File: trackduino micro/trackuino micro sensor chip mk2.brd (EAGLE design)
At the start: 49.8 x 19 mm, 41 parts, among them IC2 74AHC1G125DBV, SW1 SPST_TACT-KMR2, U1 ATMEGA168MLF, Y1 16MHZ

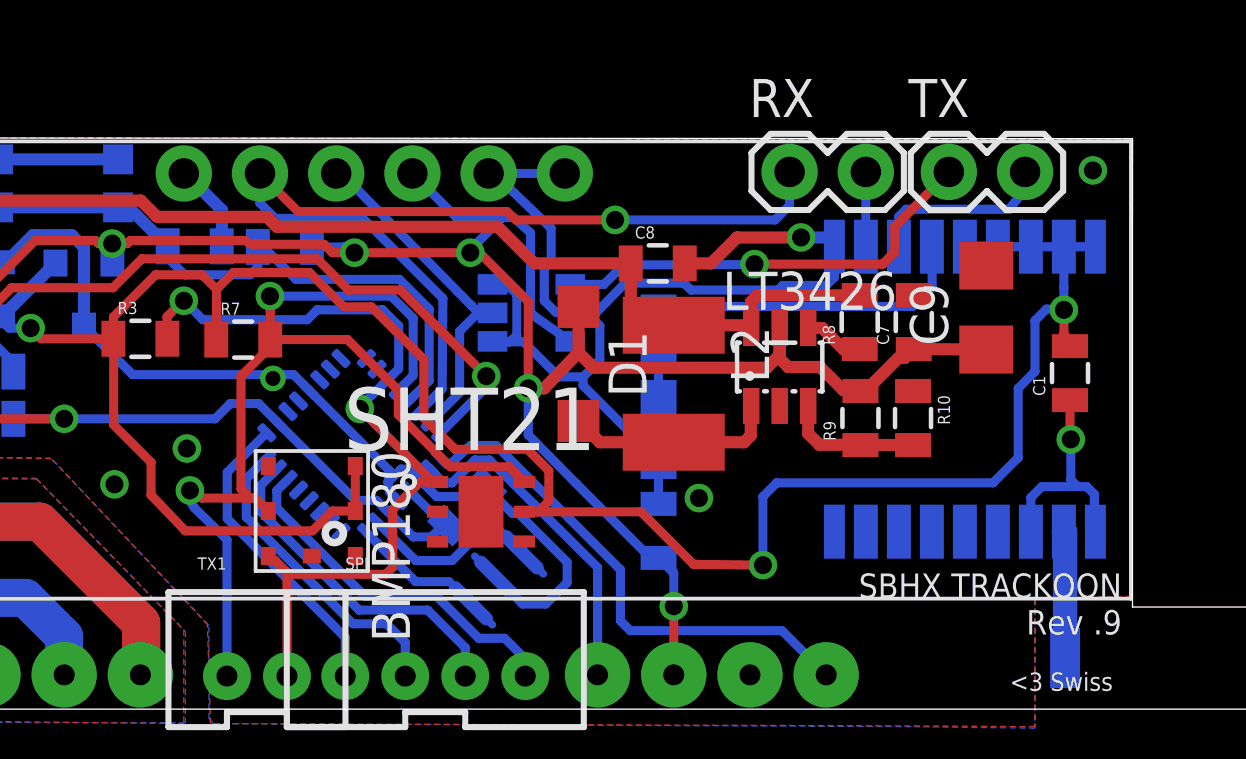
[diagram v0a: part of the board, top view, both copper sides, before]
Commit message: fixed chip serial GPS connection
Serial connection between GPS and Avr chip was not wired correctly.
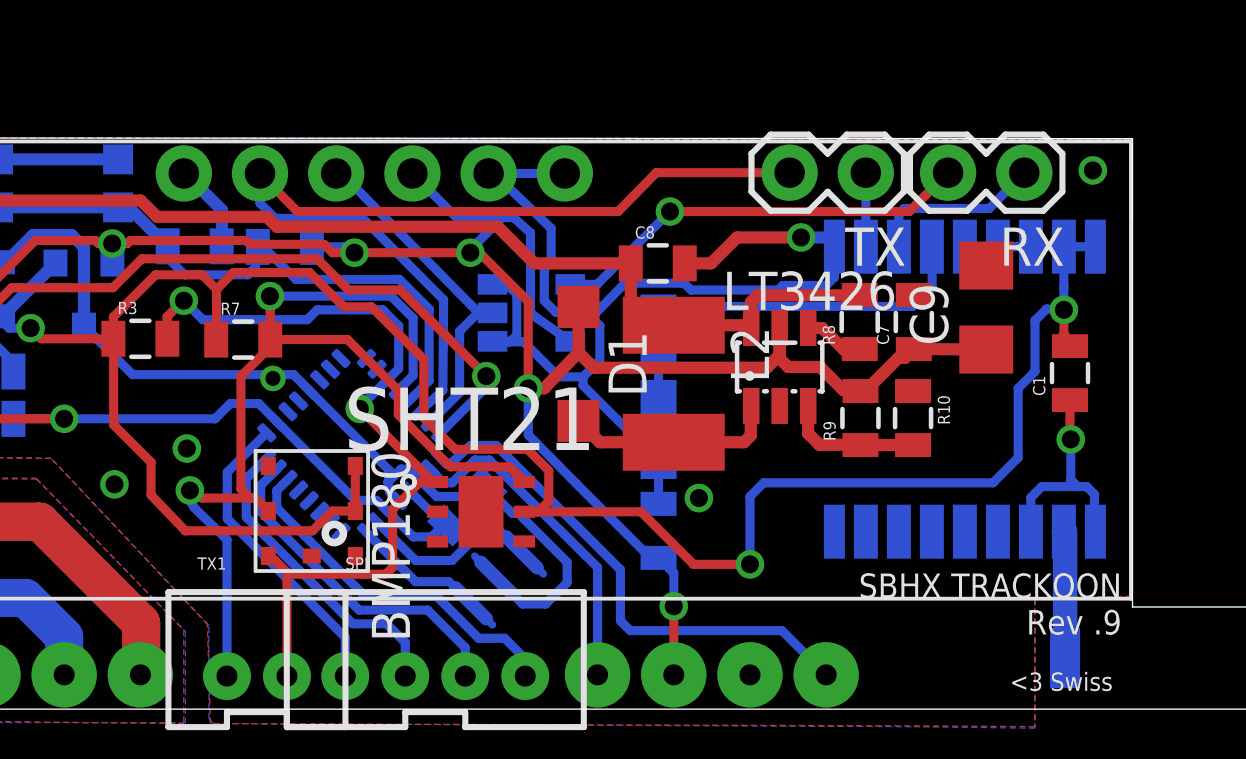
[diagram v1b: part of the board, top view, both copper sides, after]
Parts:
- moved RX 7.82 mm to (59.3, 56.7), turned to 180 degrees
- moved TX 2.77 mm to (54.0, 56.7), turned to 180 degrees
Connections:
- removed net RX: TX.2, U$1.3_RXD1
- new net RX1: RX.1, U$1.3_RXD1
- net RXO: now also TX.2; no longer RX.1
- net TX: now also TX.1; no longer RX.2
- net TX1: now also RX.2; no longer TX.1
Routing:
- net RX: track 6.21 -> 0.00 mm
- net RX1: track 0.00 -> 5.85 mm
- net RXO: track 32.1 -> 31.3 mm, vias 1 -> 0
- net TX1: track 14.7 -> 14.1 mm
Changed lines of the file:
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@@
 <element name="R5" library="SparkFun-Resistors" package="0805" value="10k" x="34.660475" y="54.193078125" rot="MR180"/>
 <element name="C5" library="SparkFun-Capacitors" package="0805" value=".1uf" x="31.654559375" y="54.213375" rot="MR0"/>
-<element name="TX" library="SparkFun-Connectors" package="1X02" value="TX" x="56.7944" y="56.6928"/>
+<element name="TX" library="SparkFun-Connectors" package="1X02" value="TX" x="54.0258" y="56.6674" rot="R180"/>
 <element name="SPI" library="SparkFun-Connectors" package="JST-4-PTH-VERT" value="" x="39.6748" y="40.4368"/>
 <element name="FRAME1" library="SparkFun-Aesthetics" package="CREATIVE_COMMONS" value="FRAME-LETTER" x="33.9598" y="30.6324"/>
@@
 <element name="U$1" library="Ava" package="UBLOX_MAX" value="UBLOX_MAX" x="57.3786" y="49.2506" rot="MR90"/>
 <element name="SW1" library="adafruit" package="KMR2" value="SPST_TACT-KMR2" x="27.1018" y="56.3118" rot="MR180"/>
-<element name="RX" library="SparkFun-Connectors" package="1X02" value="RX" x="51.4858" y="56.6928"/>
+<element name="RX" library="SparkFun-Connectors" package="1X02" value="RX" x="59.309" y="56.6674" rot="R180"/>
 <element name="BMP180" library="SparkFun-Sensors" package="BMP180" value="BMP180" x="35.56" y="45.3898" rot="R270"/>
 <element name="R3" library="SparkFun-Resistors" package="0805" value="4.7k" x="29.845" y="51.1302"/>
@@
 <wire x1="51.2318" y1="41.402" x2="52.705" y2="39.9288" width="0.3048" layer="16"/>
 </signal>
-<signal name="TX">
-<contactref element="U$1" pad="2_TXD1"/>
-<contactref element="RX" pad="2"/>
-<wire x1="54.0258" y1="56.6928" x2="54.0258" y2="54.305" width="0.3048" layer="16"/>
-<wire x1="54.0258" y1="54.305" x2="54.0286" y2="54.2006" width="0.3048" layer="16"/>
-</signal>
 <signal name="D4">
 <contactref element="U1" pad="2"/>
@@
 <via x="60.6298" y="52.0954" extent="1-16" drill="0.6" shape="square"/>
 <wire x1="60.6298" y1="52.0954" x2="60.6298" y2="51.22728125" width="0.3048" layer="1"/>
-<via x="50.5968" y="43.5864" extent="1-16" drill="0.6" shape="square"/>
-<wire x1="50.5968" y1="43.5864" x2="50.5714" y2="43.6118" width="0.3048" layer="1"/>
+<via x="50.165" y="43.6118" extent="1-16" drill="0.6" shape="square"/>
 <wire x1="60.6298" y1="51.22728125" x2="60.6298" y2="51.0904" width="0.4064" layer="1"/>
 <wire x1="60.6298" y1="51.0904" x2="60.833" y2="50.8872" width="0.4064" layer="1"/>
@@
 <wire x1="42.6466" y1="45.3644" x2="46.5328" y2="45.3644" width="0.3048" layer="1"/>
 <wire x1="46.5328" y1="45.3644" x2="48.2854" y2="43.6118" width="0.3048" layer="1"/>
-<wire x1="48.2854" y1="43.6118" x2="50.5968" y2="43.5864" width="0.3048" layer="1"/>
+<wire x1="48.2854" y1="43.6118" x2="50.165" y2="43.6118" width="0.3048" layer="1"/>
 <wire x1="37.01" y1="45.3898" x2="36.2458" y2="45.3898" width="0.3048" layer="1"/>
 <wire x1="36.2458" y1="45.3898" x2="35.5854" y2="44.7294" width="0.3048" layer="1"/>
@@
 <wire x1="40.3352" y1="47.4472" x2="39.2938" y2="48.4886" width="0.3048" layer="1"/>
 <wire x1="39.2938" y1="48.4886" x2="39.2938" y2="50.4444" width="0.3048" layer="1"/>
-<wire x1="50.5968" y1="43.5864" x2="50.5968" y2="45.8724" width="0.3048" layer="16"/>
-<wire x1="50.5968" y1="45.8724" x2="51.054" y2="46.3296" width="0.3048" layer="16"/>
-<wire x1="51.054" y1="46.3296" x2="58.2676" y2="46.3296" width="0.3048" layer="16"/>
+<wire x1="50.165" y1="43.6118" x2="50.165" y2="45.8724" width="0.3048" layer="16"/>
+<wire x1="50.165" y1="45.8724" x2="50.6222" y2="46.3296" width="0.3048" layer="16"/>
+<wire x1="50.6222" y1="46.3296" x2="58.2676" y2="46.3296" width="0.3048" layer="16"/>
 <wire x1="58.2676" y1="46.3296" x2="59.1058" y2="47.1678" width="0.3048" layer="16"/>
 <wire x1="59.1058" y1="47.1678" x2="59.1058" y2="49.4792" width="0.3048" layer="16"/>
@@
 <wire x1="47.117" y1="50.408" x2="47.117" y2="49.1576" width="0.3048" layer="16"/>
 </signal>
-<signal name="RX">
-<contactref element="U$1" pad="3_RXD1"/>
-<contactref element="TX" pad="2"/>
-<wire x1="55.1286" y1="54.2006" x2="55.1286" y2="55.2048" width="0.3048" layer="16"/>
-<wire x1="55.1286" y1="55.2048" x2="55.372" y2="55.4482" width="0.3048" layer="16"/>
-<wire x1="55.372" y1="55.4482" x2="58.801" y2="55.4482" width="0.3048" layer="16"/>
-<wire x1="58.801" y1="55.4482" x2="59.3344" y2="56.1086" width="0.3048" layer="16"/>
-<wire x1="59.3344" y1="56.1086" x2="59.3344" y2="56.6928" width="0.3048" layer="16"/>
-</signal>
 <signal name="N$8">
 <contactref element="VCC" pad="A"/>
@@
 <contactref element="U1" pad="30"/>
 <contactref element="FTDI" pad="2"/>
-<contactref element="RX" pad="1"/>
-<wire x1="39.14903125" y1="48.70556875" x2="39.9034" y2="49.4599375" width="0.3048" layer="16"/>
-<wire x1="39.9034" y1="49.4599375" x2="39.9288" y2="52.4764" width="0.3048" layer="16"/>
-<wire x1="39.9288" y1="52.4764" x2="37.2618" y2="55.1434" width="0.3048" layer="16"/>
+<wire x1="39.14903125" y1="48.70556875" x2="39.9288" y2="49.4091375" width="0.3048" layer="16"/>
+<wire x1="39.9288" y1="49.4091375" x2="39.9542" y2="52.4256" width="0.3048" layer="16"/>
+<wire x1="39.9542" y1="52.4256" x2="37.2618" y2="55.1434" width="0.3048" layer="16"/>
 <wire x1="37.2618" y1="55.1434" x2="34.3408" y2="55.1434" width="0.3048" layer="16"/>
 <wire x1="34.3408" y1="55.1434" x2="33.8328" y2="55.6514" width="0.3048" layer="16"/>
 <wire x1="33.8328" y1="55.6514" x2="33.8328" y2="56.642" width="0.3048" layer="16"/>
-<wire x1="51.4858" y1="56.6928" x2="51.4858" y2="55.5752" width="0.3048" layer="16"/>
-<wire x1="51.4858" y1="55.5752" x2="51.0032" y2="55.0926" width="0.3048" layer="16"/>
-<wire x1="51.0032" y1="55.0926" x2="45.6692" y2="55.0926" width="0.3048" layer="16"/>
-<via x="45.6692" y="55.0926" extent="1-16" drill="0.6" shape="square"/>
-<wire x1="45.6692" y1="55.0926" x2="42.3672" y2="55.0926" width="0.3048" layer="1"/>
-<wire x1="42.3672" y1="55.0926" x2="42.0624" y2="55.372" width="0.3048" layer="1"/>
-<wire x1="42.0624" y1="55.372" x2="35.1028" y2="55.372" width="0.3048" layer="1"/>
-<wire x1="35.1028" y1="55.372" x2="33.8328" y2="56.642" width="0.3048" layer="1"/>
+<contactref element="TX" pad="2"/>
+<wire x1="51.4858" y1="56.6674" x2="47.0408" y2="56.6674" width="0.3048" layer="1"/>
+<wire x1="47.0408" y1="56.6674" x2="45.7708" y2="55.372" width="0.3048" layer="1"/>
+<wire x1="45.7708" y1="55.372" x2="35.0774" y2="55.372" width="0.3048" layer="1"/>
+<wire x1="35.0774" y1="55.372" x2="33.8328" y2="56.642" width="0.3048" layer="1"/>
 </signal>
 <signal name="TXO">
@@
 <signal name="TX1">
 <contactref element="IC2" pad="4"/>
-<contactref element="TX" pad="1"/>
-<wire x1="44.1752" y1="52.9438" x2="45.2984" y2="52.9438" width="0.3048" layer="16"/>
-<wire x1="45.2984" y1="52.9438" x2="45.9486" y2="53.594" width="0.3048" layer="16"/>
-<wire x1="45.9486" y1="53.594" x2="50.3022" y2="53.6042" width="0.3048" layer="16"/>
-<wire x1="50.3022" y1="53.6042" x2="50.3174" y2="53.6194" width="0.3048" layer="16"/>
-<via x="50.3174" y="53.6194" extent="1-16" drill="0.6" shape="square"/>
-<wire x1="50.3174" y1="53.6194" x2="54.5846" y2="53.6194" width="0.3048" layer="1"/>
-<wire x1="54.5846" y1="53.6194" x2="54.991" y2="54.0258" width="0.3048" layer="1"/>
-<wire x1="54.991" y1="54.0258" x2="54.991" y2="54.864" width="0.3048" layer="1"/>
-<wire x1="54.991" y1="54.864" x2="55.372" y2="55.245" width="0.3048" layer="1"/>
-<wire x1="55.372" y1="55.245" x2="56.7944" y2="56.6928" width="0.3048" layer="1"/>
+<contactref element="RX" pad="2"/>
+<wire x1="44.1752" y1="52.9438" x2="45.0698" y2="52.9438" width="0.3048" layer="16"/>
+<wire x1="45.0698" y1="52.9438" x2="47.498" y2="55.372" width="0.3048" layer="16"/>
+<via x="47.498" y="55.372" extent="1-16" drill="0.6" shape="square"/>
+<wire x1="47.498" y1="55.372" x2="55.4736" y2="55.372" width="0.3048" layer="1"/>
+<wire x1="55.4736" y1="55.372" x2="56.769" y2="56.6674" width="0.3048" layer="1"/>
 </signal>
 <signal name="VDDD">
@@
 <wire x1="30.754559375" y1="54.213375" x2="30.754559375" y2="53.827440625" width="0.3048" layer="16"/>
 <wire x1="30.754559375" y1="53.827440625" x2="31.3182" y2="53.2638" width="0.3048" layer="16"/>
-<wire x1="31.3182" y1="53.2638" x2="33.5026" y2="53.2638" width="0.3048" layer="16"/>
-<wire x1="33.5026" y1="53.2638" x2="33.7566" y2="53.5178" width="0.3048" layer="16"/>
-<wire x1="33.7566" y1="53.5178" x2="33.7566" y2="54.189203125" width="0.3048" layer="16"/>
+<wire x1="31.3182" y1="53.2638" x2="33.4264" y2="53.2638" width="0.3048" layer="16"/>
+<wire x1="33.4264" y1="53.2638" x2="33.6804" y2="53.5178" width="0.3048" layer="16"/>
+<wire x1="33.6804" y1="53.5178" x2="33.7566" y2="54.189203125" width="0.3048" layer="16"/>
 <wire x1="33.7566" y1="54.189203125" x2="33.760475" y2="54.193078125" width="0.3048" layer="16"/>
 <wire x1="33.760475" y1="54.193078125" x2="33.944921875" y2="54.193078125" width="0.3048" layer="16"/>
@@
 <wire x1="39.4716" y1="49.73524375" x2="38.795478125" y2="49.059121875" width="0.3048" layer="16"/>
 </signal>
+<signal name="RX1">
+<contactref element="U$1" pad="3_RXD1"/>
+<contactref element="RX" pad="1"/>
+<wire x1="55.1286" y1="54.2006" x2="55.1286" y2="55.281" width="0.3048" layer="16"/>
+<wire x1="55.1286" y1="55.281" x2="55.2958" y2="55.4736" width="0.3048" layer="16"/>
+<wire x1="55.2958" y1="55.4736" x2="58.1406" y2="55.4736" width="0.3048" layer="16"/>
+<wire x1="58.1406" y1="55.4736" x2="59.309" y2="56.6674" width="0.3048" layer="16"/>
+</signal>
+<signal name="TX">
+<contactref element="U$1" pad="2_TXD1"/>
+<contactref element="TX" pad="1"/>
+<wire x1="54.0258" y1="56.6674" x2="54.0258" y2="54.2034" width="0.3048" layer="16"/>
+<wire x1="54.0258" y1="54.2034" x2="54.0286" y2="54.2006" width="0.3048" layer="16"/>
+</signal>
 </signals>

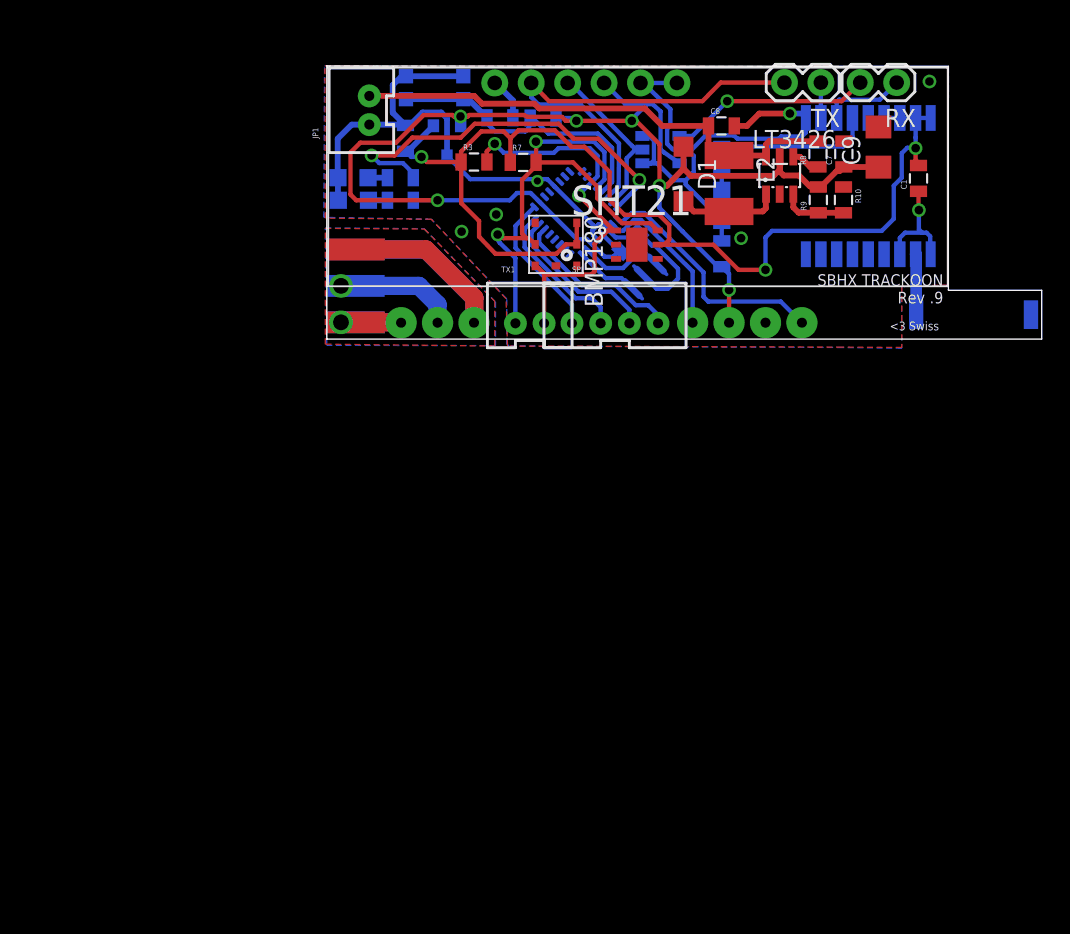
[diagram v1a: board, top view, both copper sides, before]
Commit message: Moved all boards to origin
Moved all the boards such that the lower left most corner is at the
origin.
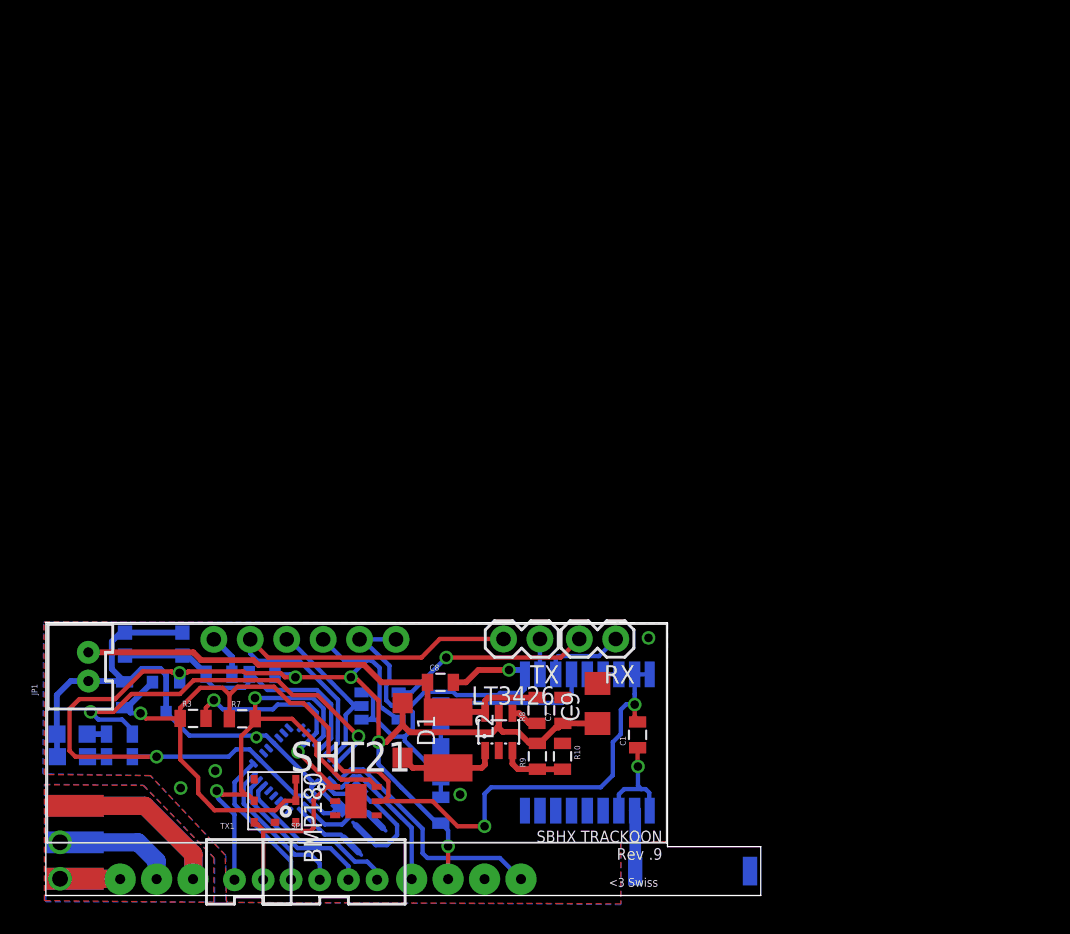
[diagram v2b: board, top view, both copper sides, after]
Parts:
- moved BMP180 43.4 mm to (16.0, 6.60)
- moved C1 43.4 mm to (41.2, 11.2)
- moved C3 43.4 mm to (21.2, 6.76)
- moved C5 43.4 mm to (12.1, 15.4)
- moved C7 43.4 mm to (36.0, 12.9)
- moved D1 43.4 mm to (24.9, 11.5)
- moved FRAME1 43.4 mm to (14.4, -8.15)
- moved FTDI 43.4 mm to (11.7, 17.9)
- moved IC2 43.4 mm to (23.3, 13.2)
- moved J$1 43.4 mm to (2.01, 1.17)
- moved JP1 43.4 mm to (2.41, 16.0)
- moved LM3480 43.4 mm to (8.38, 13.9)
- moved R1 43.4 mm to (27.5, 12.5)
- moved R3 43.4 mm to (10.3, 12.3)
- moved R4 43.4 mm to (5.13, 9.68)
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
